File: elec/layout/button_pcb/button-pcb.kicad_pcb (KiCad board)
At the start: 2 copper layers, 43.2 x 43.2 mm, 27 parts

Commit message: updated button code for readability
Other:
- board text added: "B G"
- board text added: "GlowLight/GlowTower Button PCB v2.0"
- board text added: "V D"
- board text removed: "locked"

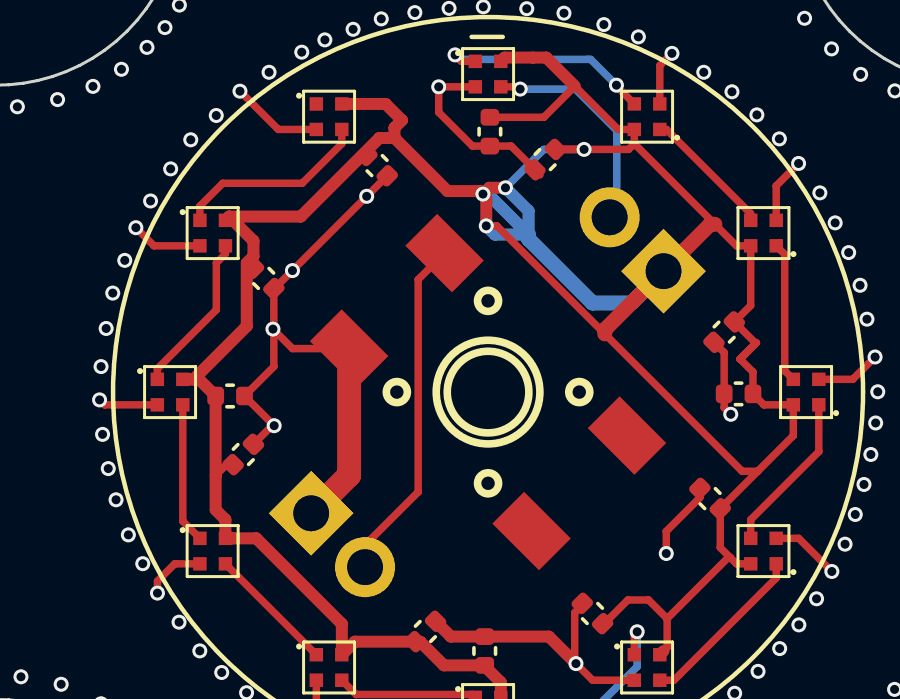
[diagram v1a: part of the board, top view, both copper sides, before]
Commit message: moved big caps for button pcb led ring to button pcb
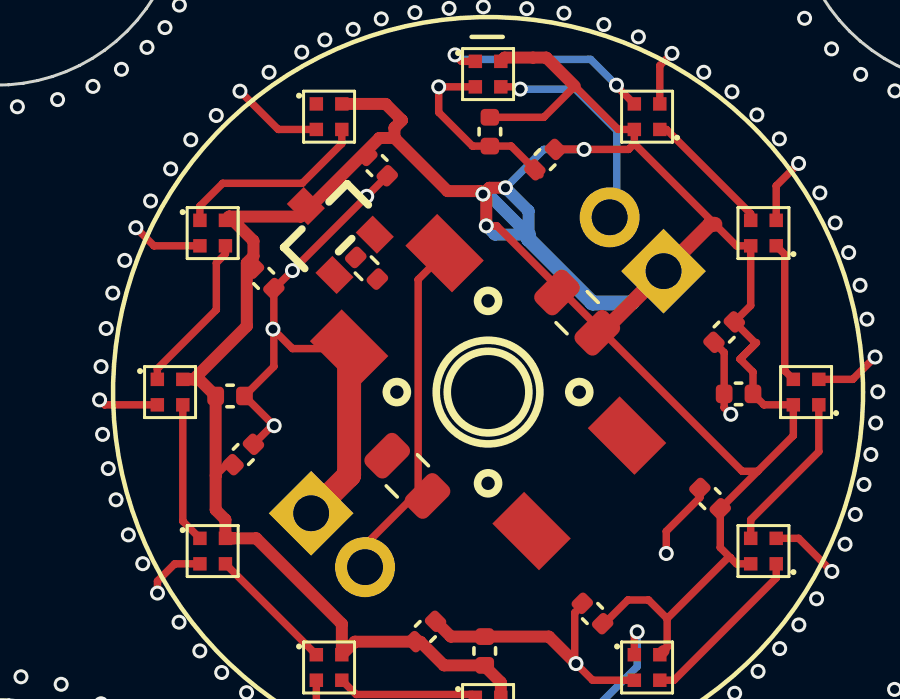
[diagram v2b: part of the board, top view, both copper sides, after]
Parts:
- added C24: , lib:C0805, F.Cu at (94.0, 64.0)
- added C24: , lib:C0805, F.Cu at (99.6, 58.6)
- added R6: None, lib:R0402, F.Cu at (92.6, 57.1)
- added U9: , lib:SOT-23_L2.9-W1.3-P1.90-LS2.4-BR, F.Cu at (91.4, 55.9)

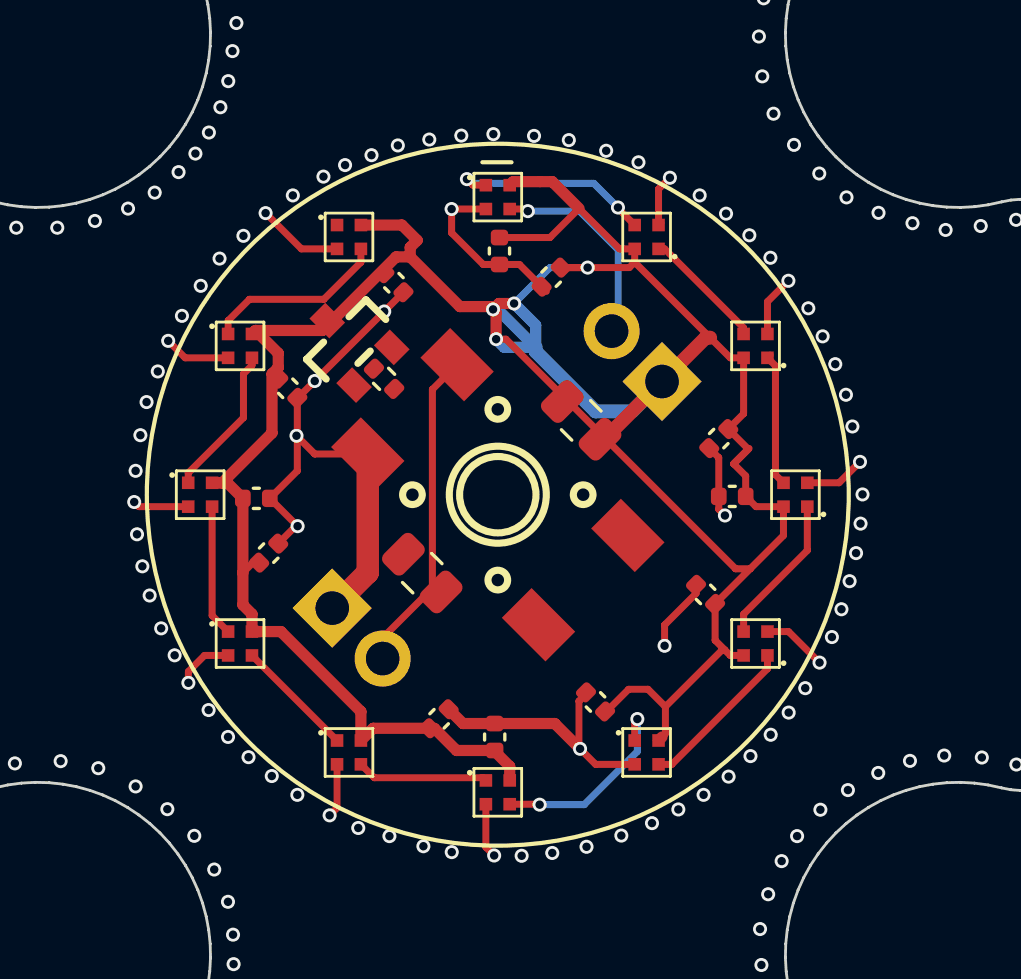
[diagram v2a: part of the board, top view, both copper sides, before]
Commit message: removed reverse polarity protection again from button pcb, because it didn't made any sense (both pin headers were 5V, so it wouldn't have worked).
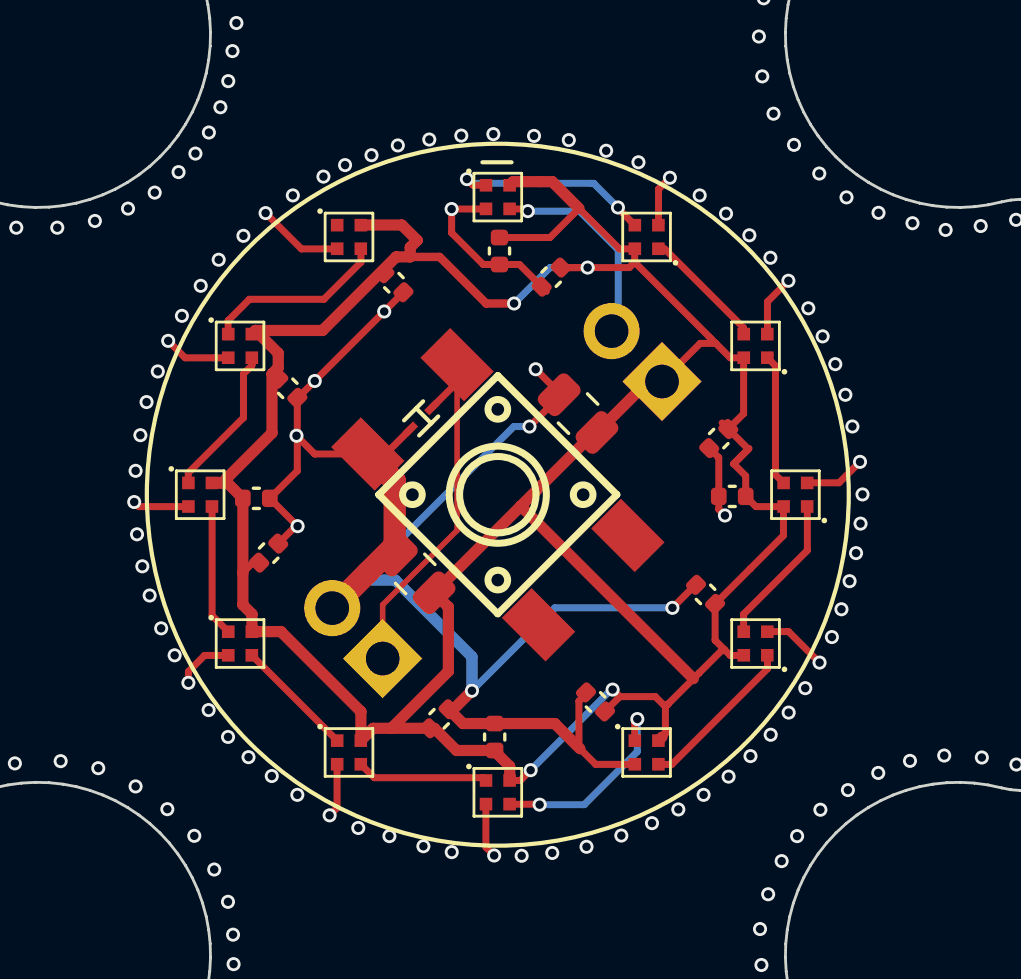
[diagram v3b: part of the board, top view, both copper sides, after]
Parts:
- removed C24 (x2): , lib:C0805
- removed R6: None, lib:R0402
- removed the U1 at (96.7, 50.6)
- removed the U2 at (102.0, 52.1)
- removed the U9 at (91.4, 55.9)
- removed the U9 at (87.5, 66.5)
- added C13: , lib:C0805, F.Cu at (99.5, 58.4)
- added C14: , lib:C0805, F.Cu at (93.7, 64.1)
- added U13: , lib:LED-SMD_4P-L1.0-W1.0-TL_XL-1010RGBC-WS2812B, F.Cu at (87.5, 55.9)
- added U14: , lib:LED-SMD_4P-L1.0-W1.0-TL_XL-1010RGBC-WS2812B, F.Cu at (91.4, 52.1)
- added U16: , lib:SOD-923_L0.8-W0.6-LS1.0-RD, F.Cu at (93.9, 58.5)
- added U9: , lib:LED-SMD_4P-L1.0-W1.0-TL_XL-1010RGBC-WS2812B, F.Cu at (96.7, 71.8)
- U10, U11, U12, U3, U4, U5, U6, U7, U8: footprint footprint:LED-SMD_4P-L1.0-W1.0-TL_XL-1010RGBC-WS2812B -> lib:LED-SMD_4P-L1.0-W1.0-TL_XL-1010RGBC-WS2812B
- U15: renamed from U13; footprint footprint:KEY-SMD_4P-L6.0-W6.0-P4.50-LS8.6 -> lib:KEY-SMD_4P-L6.0-W6.0-P4.50-LS8.6
- moved U12 10.6 mm to (86.1, 61.2)
- moved U4 10.6 mm to (102.0, 52.1)
- moved U3 10.6 mm to (96.7, 50.6), turned to 0 degrees
- moved U7 10.6 mm to (105.8, 66.5), turned to 180 degrees
- moved U10 10.6 mm to (91.4, 70.4)
- moved U6 10.6 mm to (107.3, 61.2), turned to 180 degrees
- moved U11 10.6 mm to (87.5, 66.5)
- moved U5 10.6 mm to (105.8, 55.9)
- moved U8 10.6 mm to (102.0, 70.4)
- turned U2 to 135 degrees
- renumbered U14 to U1, U15 to U2
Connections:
- net DOUT-10 renamed leds.led_9.ic-din
- net DOUT-2 renamed leds.led_1.ic-din
- net DOUT-3 renamed leds.led_2.ic-din
- net DOUT-4 renamed leds.led_3.ic-din
- net DOUT-5 renamed leds.led_4.ic-din
- net DOUT-6 renamed leds.led_5.ic-din
- net DOUT-9 renamed leds.led_8.ic-din
- net _2 renamed p2
- net _4 renamed p4
- U1 pad 2: DIN -> data
- U10 pad 4: DOUT-8 -> leds.led_7.ic-din
- U12 pad 1: DOUT-11 -> leds.led_10.ic-din
- U15 pad 1: _1 -> input
- U2 pad 1: gnd -> input
- U2 pad 2: _1 -> gnd
- U3 pad 4: DOUT-1 -> data
- U8 pad 1: DOUT-7 -> leds.led_6.ic-din
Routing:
- net gnd: track 63.7 -> 94.8 mm, vias 196 -> 198
- net input: track 0.00 -> 14.2 mm
- net _1: track 11.6 -> 0.00 mm
- net data: track 0.00 -> 7.46 mm, vias 0 -> 1
- net DIN: track 7.46 -> 0.00 mm, vias 1 -> 0
- net DOUT: track 7.43 -> 0.00 mm, vias 2 -> 0
- net leds.led_6.ic-din: track 0.00 -> 7.30 mm, vias 0 -> 2
- net leds.led_11.ic-din: track 0.00 -> 6.54 mm
- net leds.led_10.ic-din: track 0.00 -> 5.39 mm
- net DOUT-8: track 4.69 -> 0.00 mm
- net leds.led_7.ic-din: track 0.00 -> 4.69 mm
- net DOUT-1: track 4.49 -> 0.00 mm
- net DOUT-7: track 4.29 -> 0.00 mm
- net vcc: track 114.7 -> 118.8 mm
- net leds.led_1.ic-din: track 4.82 -> 7.43 mm, vias 0 -> 2
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
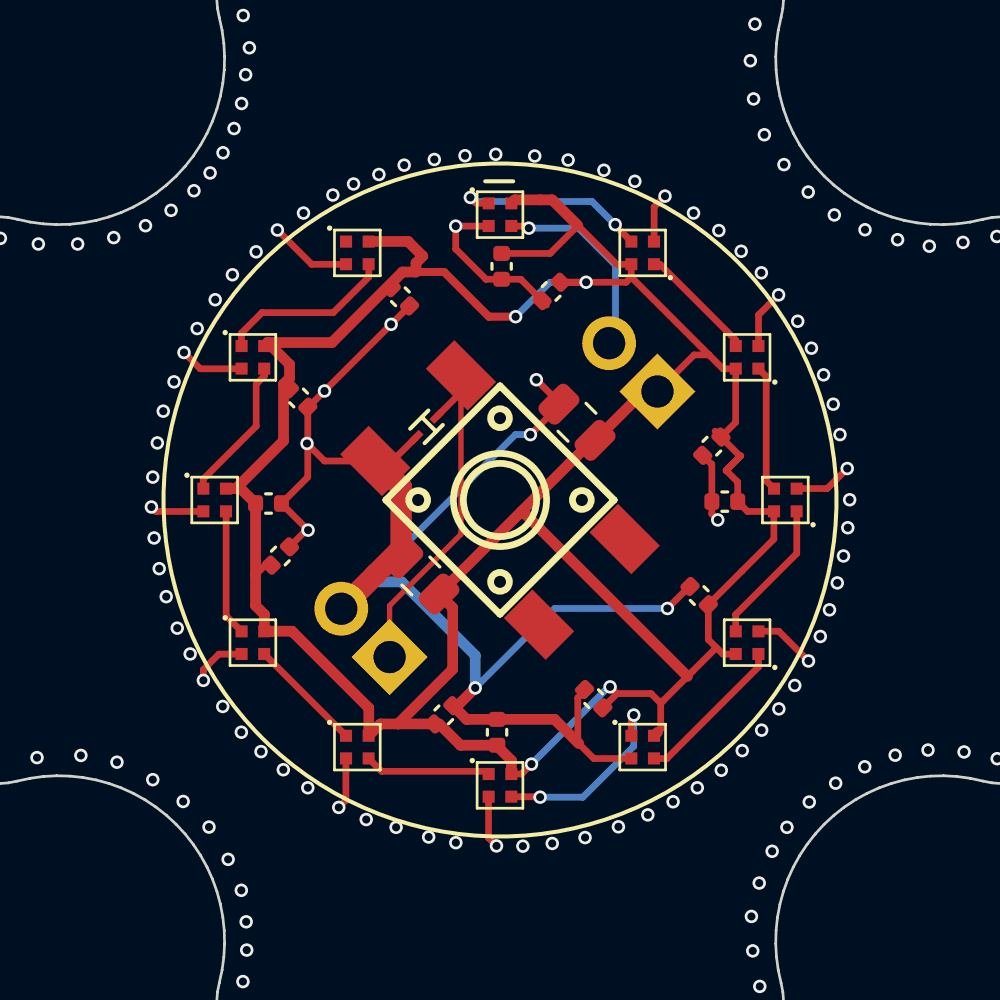
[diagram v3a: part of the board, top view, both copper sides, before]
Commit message: updated button pcb and replaced 3d models with .step files
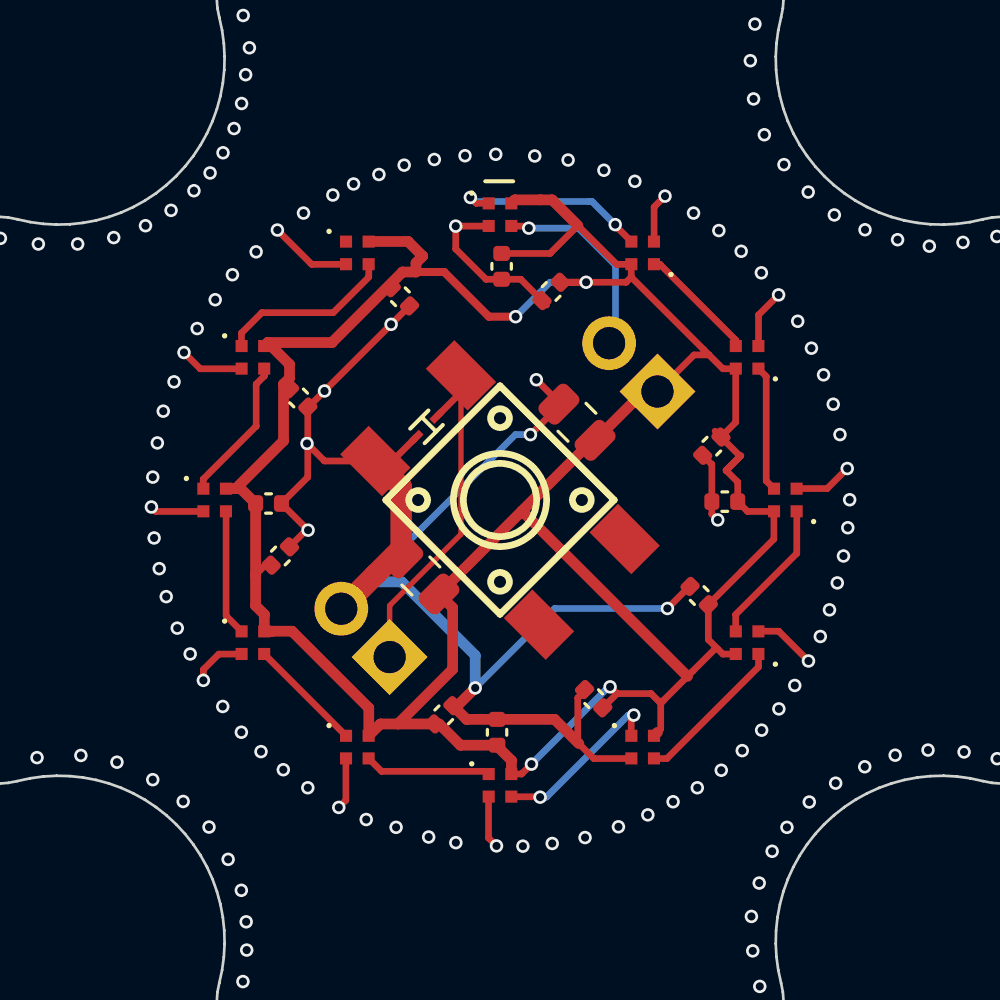
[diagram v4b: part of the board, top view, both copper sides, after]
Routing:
- net leds.led_6.ic-din: track 7.30 -> 6.62 mm
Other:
- board text added: "5V | D"
- board text added: "B | G"
- board text added: "Button"
- board text added: "GlowLight/GlowTower Button PCB v3.0"
- board text added: "LEDs"
- board text added: "bit.ly/3P7PfLo"
- board text removed: "B G"
- board text removed: "GlowLight/GlowTower Button PCB v2.0"
- board text removed: "V D"

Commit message: added githash to button pcb
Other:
- board text added: "{{GITHASH}}"

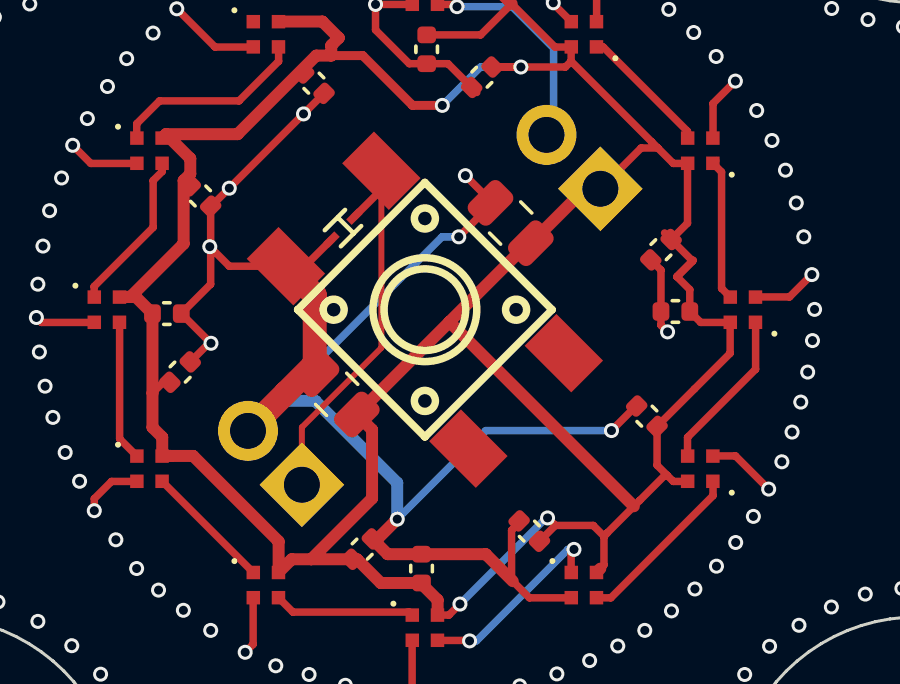
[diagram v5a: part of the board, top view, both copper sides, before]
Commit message: moved led ring capacitor back to main pcb, added mounting holes to .ato file
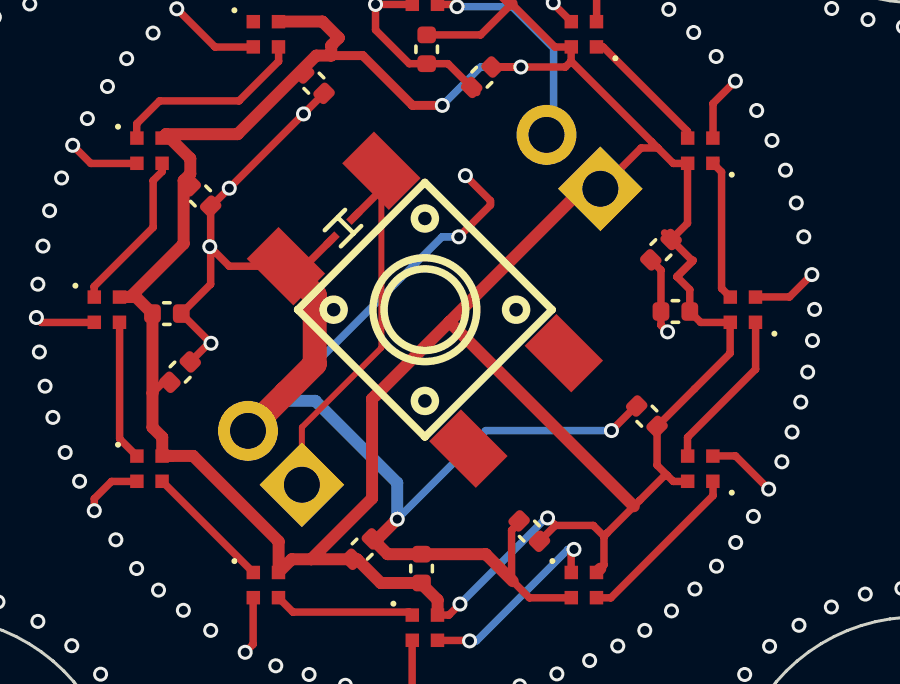
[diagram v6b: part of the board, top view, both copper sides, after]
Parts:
- removed C13, C14: , lib:C0805

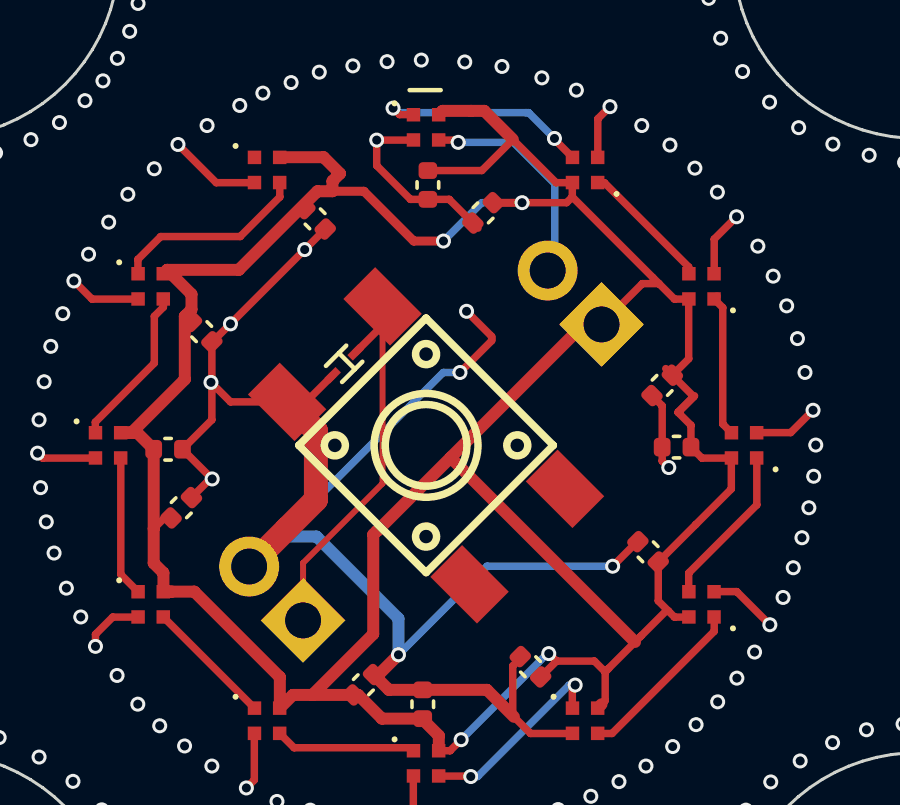
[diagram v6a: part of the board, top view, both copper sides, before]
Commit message: updated button pcb, removed caps
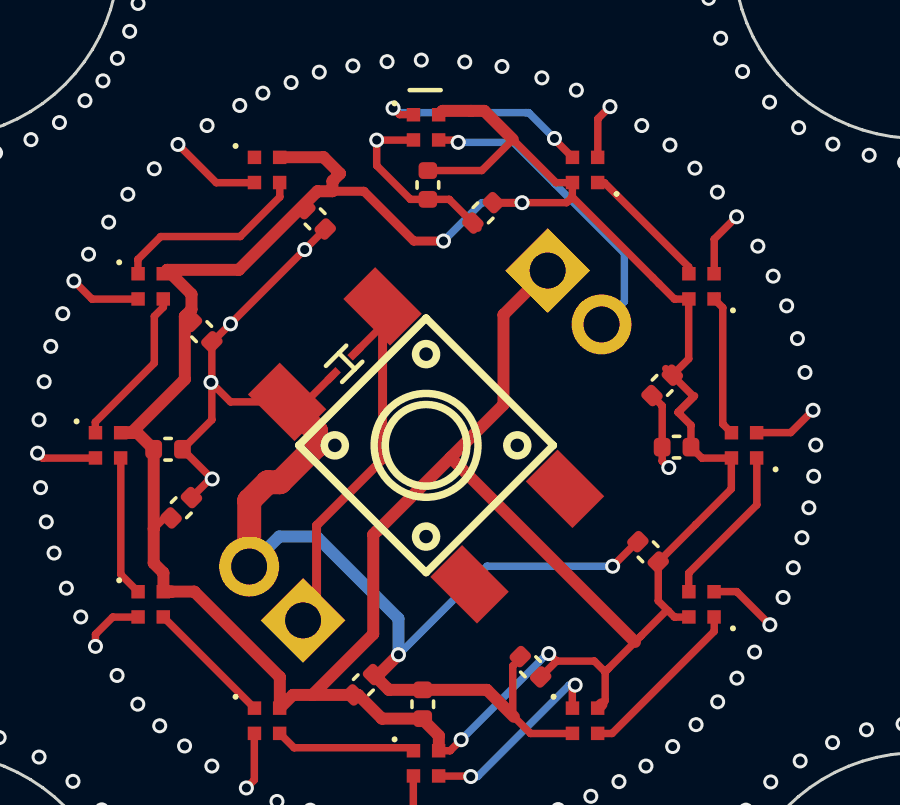
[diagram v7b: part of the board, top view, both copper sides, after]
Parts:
- turned U1 to -45 degrees
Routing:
- net gnd: track 94.8 -> 82.5 mm, vias 198 -> 196
- net data: track 7.46 -> 11.5 mm
- net vcc: track 118.6 -> 116.6 mm
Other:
- board text added: "D | 5V"
- board text removed: "5V | D"
